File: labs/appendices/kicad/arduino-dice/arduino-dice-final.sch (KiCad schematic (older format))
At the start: 10 parts, among them IC1 ATMEGA328P-P, P1 CONN_01X02, SW1 SW_PUSH, Y1 16 MHz

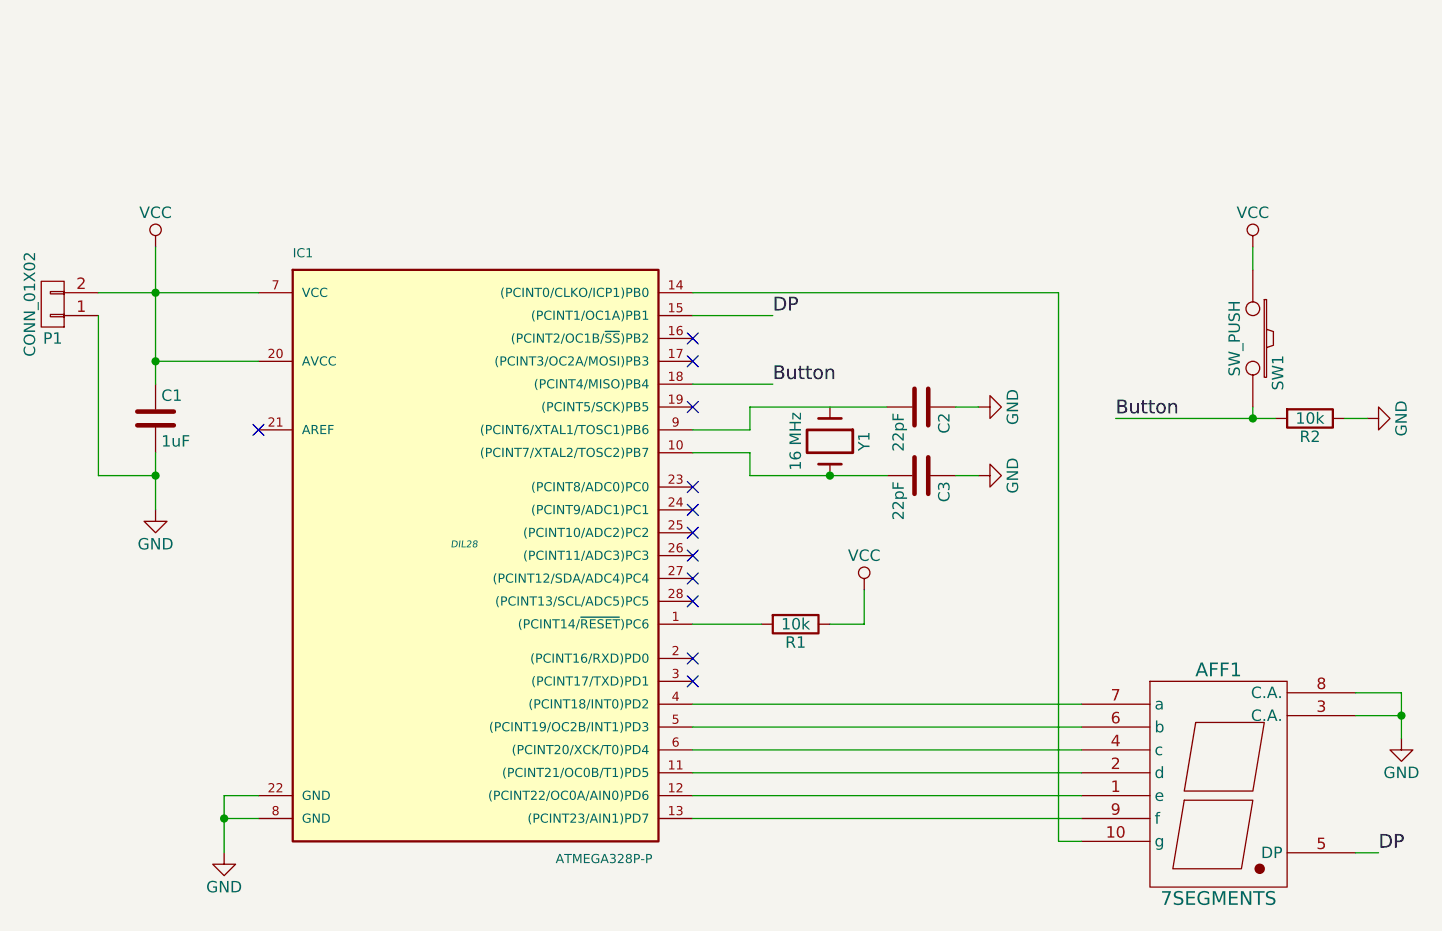
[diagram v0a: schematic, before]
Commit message: update pcb tutorial
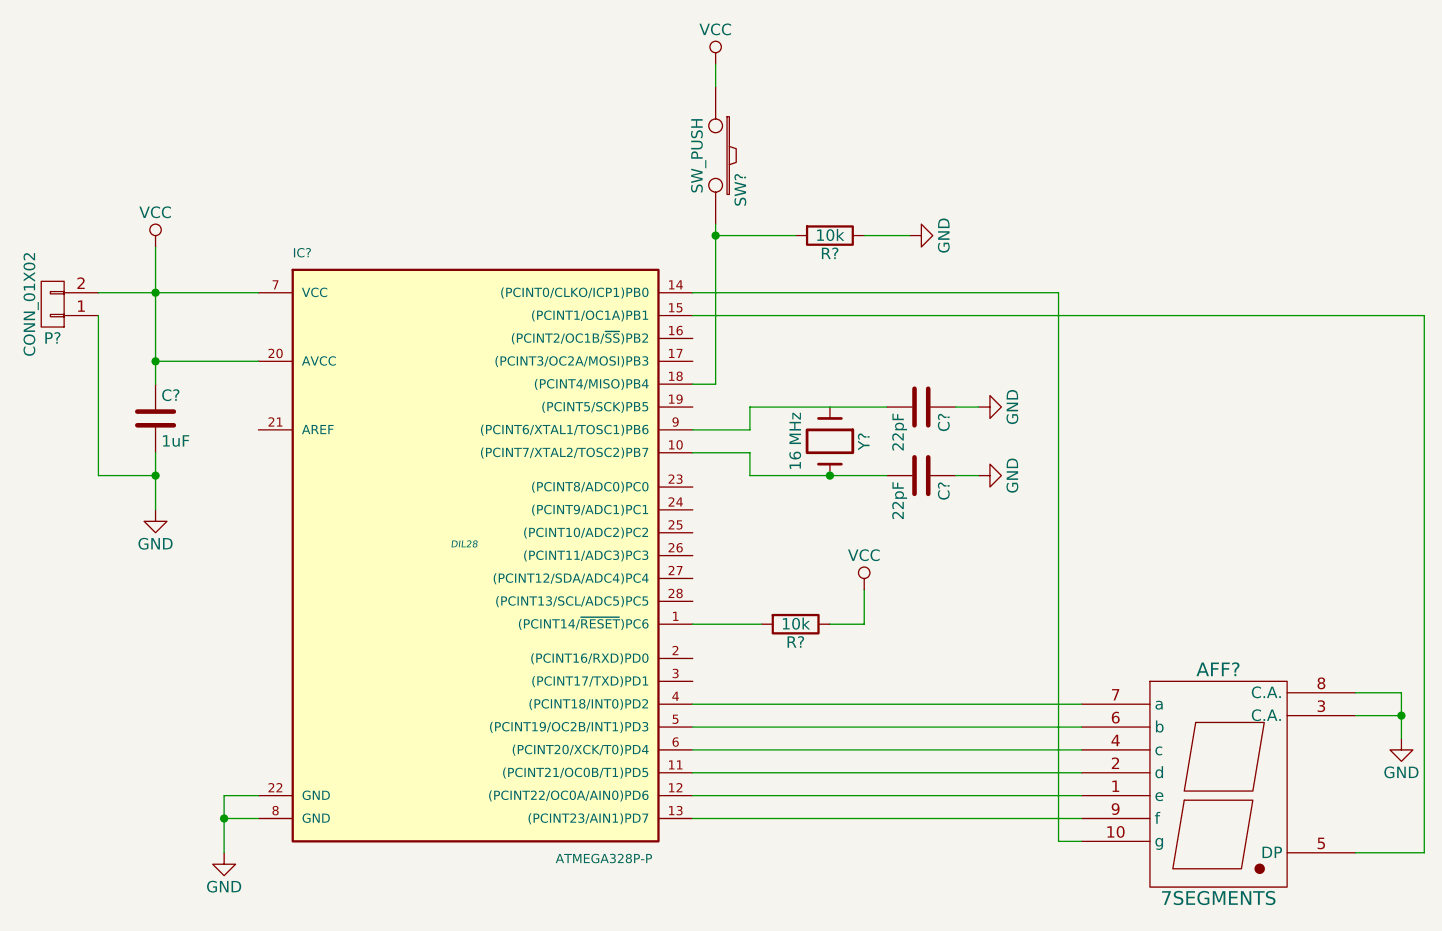
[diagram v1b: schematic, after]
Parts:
- renumbered AFF1 to AFF?, C2 to C?, C3 to C?, C1 to C?, IC1 to IC?, P1 to P?, R2 to R?, R1 to R?, SW1 to SW?, Y1 to Y?
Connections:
- net Button: no longer names the net of IC?.18 ((PCINT4/MISO)PB4), R?.2, SW?.2
- net DP: no longer names the net of AFF?.5 (DP), IC?.15 ((PCINT1/OC1A)PB1)
- no-connect marks 12 -> 0
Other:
- moved on the sheet: R?, SW?
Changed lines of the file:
@@
 $EndDescr
 $Comp
-L ATMEGA328P-P IC1
+L ATMEGA328P-P IC?
 U 1 1 55CE75F6
 P 3300 3450
-F 0 "IC1" H 2550 4700 40  0000 L BNN
+F 0 "IC?" H 2550 4700 40  0000 L BNN
 F 1 "ATMEGA328P-P" H 3700 2050 40  0000 L BNN
 F 2 "DIL28" H 3300 3450 30  0000 C CIN
@@
 $EndComp
 $Comp
-L R R2
+L R R?
 U 1 1 55CE77A0
-P 7000 2900
-F 0 "R2" V 7080 2900 50  0000 C CNN
-F 1 "10k" V 7000 2900 50  0000 C CNN
-F 2 "" V 6930 2900 30  0000 C CNN
-F 3 "" H 7000 2900 30  0000 C CNN
-	1    7000 2900
-	0    1    1    0
-$EndComp
-$Comp
-L 7SEGMENTS AFF1
+P 4900 2100
+F 0 "R?" V 4980 2100 50  0000 C CNN
+F 1 "10k" V 4900 2100 50  0000 C CNN
+F 2 "" V 4830 2100 30  0000 C CNN
+F 3 "" H 4900 2100 30  0000 C CNN
+	1    4900 2100
+	0    1    1    0
+$EndComp
+$Comp
+L 7SEGMENTS AFF?
 U 1 1 55CE7823
 P 6600 4550
-F 0 "AFF1" H 6600 5100 60  0000 C CNN
+F 0 "AFF?" H 6600 5100 60  0000 C CNN
 F 1 "7SEGMENTS" H 6600 4100 60  0000 C CNN
 F 2 "" H 6600 4550 60  0000 C CNN
@@
 $EndComp
 $Comp
-L R R1
+L R R?
 U 1 1 55CE7957
 P 4750 3800
-F 0 "R1" V 4830 3800 50  0000 C CNN
+F 0 "R?" V 4830 3800 50  0000 C CNN
 F 1 "10k" V 4750 3800 50  0000 C CNN
 F 2 "" V 4680 3800 30  0000 C CNN
@@
 $EndComp
 $Comp
-L Crystal Y1
+L Crystal Y?
 U 1 1 55CE79BA
 P 4900 3000
-F 0 "Y1" H 4900 3150 50  0000 C CNN
+F 0 "Y?" H 4900 3150 50  0000 C CNN
 F 1 "16 MHz" H 4900 2850 50  0000 C CNN
 F 2 "" H 4900 3000 60  0000 C CNN
@@
 $EndComp
 $Comp
-L C C2
+L C C?
 U 1 1 55CE7AFB
 P 5300 2850
-F 0 "C2" H 5325 2950 50  0000 L CNN
+F 0 "C?" H 5325 2950 50  0000 L CNN
 F 1 "22pF" H 5325 2750 50  0000 L CNN
 F 2 "" H 5338 2700 30  0000 C CNN
@@
 $EndComp
 $Comp
-L C C3
+L C C?
 U 1 1 55CE7BE8
 P 5300 3150
-F 0 "C3" H 5325 3250 50  0000 L CNN
+F 0 "C?" H 5325 3250 50  0000 L CNN
 F 1 "22pF" H 5325 3050 50  0000 L CNN
 F 2 "" H 5338 3000 30  0000 C CNN
@@
 $EndComp
 $Comp
-L SW_PUSH SW1
+L SW_PUSH SW?
 U 1 1 55CE7E1C
-P 6750 2550
-F 0 "SW1" H 6900 2660 50  0000 C CNN
-F 1 "SW_PUSH" H 6750 2470 50  0000 C CNN
-F 2 "" H 6750 2550 60  0000 C CNN
-F 3 "" H 6750 2550 60  0000 C CNN
-	1    6750 2550
+P 4400 1750
+F 0 "SW?" H 4550 1860 50  0000 C CNN
+F 1 "SW_PUSH" H 4400 1670 50  0000 C CNN
+F 2 "" H 4400 1750 60  0000 C CNN
+F 3 "" H 4400 1750 60  0000 C CNN
+	1    4400 1750
 	0    1    1    0
 $EndComp
@@
 Connection ~ 4900 3150
 Wire Wire Line
-	4650 2750 4300 2750
-Wire Wire Line
-	6150 2900 6850 2900
+	4400 2050 4400 2750
+Wire Wire Line
+	4400 2750 4300 2750
+Wire Wire Line
+	4750 2100 4400 2100
+Connection ~ 4400 2100
 Wire Wire Line
 	6000 4650 4300 4650
@@
 	5900 4750 6000 4750
 $Comp
-L GND #PWR01
+L GND #PWR?
 U 1 1 55CE8044
 P 5550 2850
-F 0 "#PWR01" H 5550 2600 50  0001 C CNN
+F 0 "#PWR?" H 5550 2600 50  0001 C CNN
 F 1 "GND" H 5550 2700 50  0000 C CNN
 F 2 "" H 5550 2850 60  0000 C CNN
@@
 $EndComp
 $Comp
-L GND #PWR02
+L GND #PWR?
 U 1 1 55CE8140
 P 5550 3150
-F 0 "#PWR02" H 5550 2900 50  0001 C CNN
+F 0 "#PWR?" H 5550 2900 50  0001 C CNN
 F 1 "GND" H 5550 3000 50  0000 C CNN
 F 2 "" H 5550 3150 60  0000 C CNN
@@
 	5450 3150 5550 3150
 $Comp
-L C C1
+L C C?
 U 1 1 55CE8287
 P 1950 2900
-F 0 "C1" H 1975 3000 50  0000 L CNN
+F 0 "C?" H 1975 3000 50  0000 L CNN
 F 1 "1uF" H 1975 2800 50  0000 L CNN
 F 2 "" H 1988 2750 30  0000 C CNN
@@
 $EndComp
 $Comp
-L CONN_01X02 P1
+L CONN_01X02 P?
 U 1 1 55CE837D
 P 1500 2400
-F 0 "P1" H 1500 2550 50  0000 C CNN
+F 0 "P?" H 1500 2550 50  0000 C CNN
 F 1 "CONN_01X02" V 1600 2400 50  0000 C CNN
 F 2 "" H 1500 2400 60  0000 C CNN
@@
 	1950 2650 2400 2650
 $Comp
-L VCC #PWR03
+L VCC #PWR?
 U 1 1 55CE8600
 P 1950 2150
-F 0 "#PWR03" H 1950 2000 50  0001 C CNN
+F 0 "#PWR?" H 1950 2000 50  0001 C CNN
 F 1 "VCC" H 1950 2300 50  0000 C CNN
 F 2 "" H 1950 2150 60  0000 C CNN
@@
 Connection ~ 1950 2650
 $Comp
-L VCC #PWR04
+L VCC #PWR?
 U 1 1 55CE88AC
-P 6750 2150
-F 0 "#PWR04" H 6750 2000 50  0001 C CNN
-F 1 "VCC" H 6750 2300 50  0000 C CNN
-F 2 "" H 6750 2150 60  0000 C CNN
-F 3 "" H 6750 2150 60  0000 C CNN
-	1    6750 2150
-	1    0    0    -1
-$EndComp
-Wire Wire Line
-	6750 2150 6750 2250
-$Comp
-L GND #PWR05
+P 4400 1350
+F 0 "#PWR?" H 4400 1200 50  0001 C CNN
+F 1 "VCC" H 4400 1500 50  0000 C CNN
+F 2 "" H 4400 1350 60  0000 C CNN
+F 3 "" H 4400 1350 60  0000 C CNN
+	1    4400 1350
+	1    0    0    -1
+$EndComp
+Wire Wire Line
+	4400 1350 4400 1450
+$Comp
+L GND #PWR?
 U 1 1 55CE8A84
 P 1950 3300
-F 0 "#PWR05" H 1950 3050 50  0001 C CNN
+F 0 "#PWR?" H 1950 3050 50  0001 C CNN
 F 1 "GND" H 1950 3150 50  0000 C CNN
 F 2 "" H 1950 3300 60  0000 C CNN
@@
 Connection ~ 1950 3150
 $Comp
-L GND #PWR06
+L GND #PWR?
 U 1 1 55CE8CEC
 P 2250 4800
-F 0 "#PWR06" H 2250 4550 50  0001 C CNN
+F 0 "#PWR?" H 2250 4550 50  0001 C CNN
 F 1 "GND" H 2250 4650 50  0000 C CNN
 F 2 "" H 2250 4800 60  0000 C CNN
@@
 Connection ~ 2250 4650
 $Comp
-L VCC #PWR07
+L VCC #PWR?
 U 1 1 55CE8F1D
 P 5050 3650
-F 0 "#PWR07" H 5050 3500 50  0001 C CNN
+F 0 "#PWR?" H 5050 3500 50  0001 C CNN
 F 1 "VCC" H 5050 3800 50  0000 C CNN
 F 2 "" H 5050 3650 60  0000 C CNN
@@
 	4600 3800 4300 3800
 $Comp
-L GND #PWR08
+L GND #PWR?
 U 1 1 55CE9051
 P 7400 4300
-F 0 "#PWR08" H 7400 4050 50  0001 C CNN
+F 0 "#PWR?" H 7400 4050 50  0001 C CNN
 F 1 "GND" H 7400 4150 50  0000 C CNN
 F 2 "" H 7400 4300 60  0000 C CNN
@@
 Connection ~ 7400 4200
 Wire Wire Line
-	7300 4800 7200 4800
-$Comp
-L GND #PWR09
+	4300 2450 7500 2450
+Wire Wire Line
+	7500 2450 7500 4800
+Wire Wire Line
+	7500 4800 7200 4800
+$Comp
+L GND #PWR?
 U 1 1 55CE94EA
-P 7250 2900
-F 0 "#PWR09" H 7250 2650 50  0001 C CNN
-F 1 "GND" H 7250 2750 50  0000 C CNN
-F 2 "" H 7250 2900 60  0000 C CNN
-F 3 "" H 7250 2900 60  0000 C CNN
-	1    7250 2900
+P 5250 2100
+F 0 "#PWR?" H 5250 1850 50  0001 C CNN
+F 1 "GND" H 5250 1950 50  0000 C CNN
+F 2 "" H 5250 2100 60  0000 C CNN
+F 3 "" H 5250 2100 60  0000 C CNN
+	1    5250 2100
 	0    -1   -1   0
 $EndComp
 Wire Wire Line
-	7250 2900 7150 2900
-Wire Wire Line
-	4300 2450 4650 2450
-Text Label 4650 2450 0    60   ~ 0
-DP
-NoConn ~ 4300 2550
-NoConn ~ 4300 2650
-NoConn ~ 4300 2850
-NoConn ~ 4300 3200
-NoConn ~ 4300 3300
-NoConn ~ 4300 3400
-NoConn ~ 4300 3500
-NoConn ~ 4300 3600
-NoConn ~ 4300 3700
-NoConn ~ 4300 3950
-NoConn ~ 4300 4050
-NoConn ~ 2400 2950
-Text Label 4650 2750 0    60   ~ 0
-Button
-Text Label 7300 4800 0    60   ~ 0
-DP
-Wire Wire Line
-	6750 2850 6750 2900
-Connection ~ 6750 2900
-Text Label 6150 2900 0    60   ~ 0
-Button
+	5250 2100 5050 2100
 $EndSCHEMATC
